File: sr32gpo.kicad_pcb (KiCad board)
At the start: 2 copper layers, 99.1 x 66 mm, 68 parts, among them J1 Power, J11 GPO, J12 GPO, J13 GND, J2 Power, J21 GPO, J22 GPO, J23 GND, J3 Power, J31 GPO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

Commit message: Redo with updated SOIC-16 footprint, better GND planes, and tentative fields for PCBWay assembly. Unverified.
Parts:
- U1, U2, U3, U4: footprint Package_SO:SO-16_3.9x9.9mm_P1.27mm -> Package_SO:SOIC-16_3.9x9.9mm_P1.27mm
- U11: value LD1117 -> LD1117V33
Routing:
- net /V+: track 47.1 -> 35.2 mm
- net VCC: track 155.3 -> 144.6 mm
- net /~{SRCLR}: track 81.4 -> 70.7 mm, vias 1 -> 0
- net GND: track 342.4 -> 352.2 mm, vias 1 -> 3
- net /RCLK: track 74.5 -> 67.8 mm, vias 1 -> 3
- net Net-(U1-Pad9): track 5.10 -> 10.9 mm
- net Net-(R22-Pad1): track 9.59 -> 4.58 mm
- net /~{OE}: track 62.5 -> 58.1 mm, vias 2 -> 1
- net Net-(U3-Pad9): track 12.8 -> 9.38 mm, vias 0 -> 2
- net Net-(R11-Pad1): track 14.0 -> 12.3 mm, vias 0 -> 2
- net /SRCLK: track 73.3 -> 72.2 mm, vias 3 -> 2
- net Net-(R41-Pad1): track 20.9 -> 20.2 mm
- net Net-(R21-Pad1): track 14.6 -> 15.3 mm, vias 0 -> 2

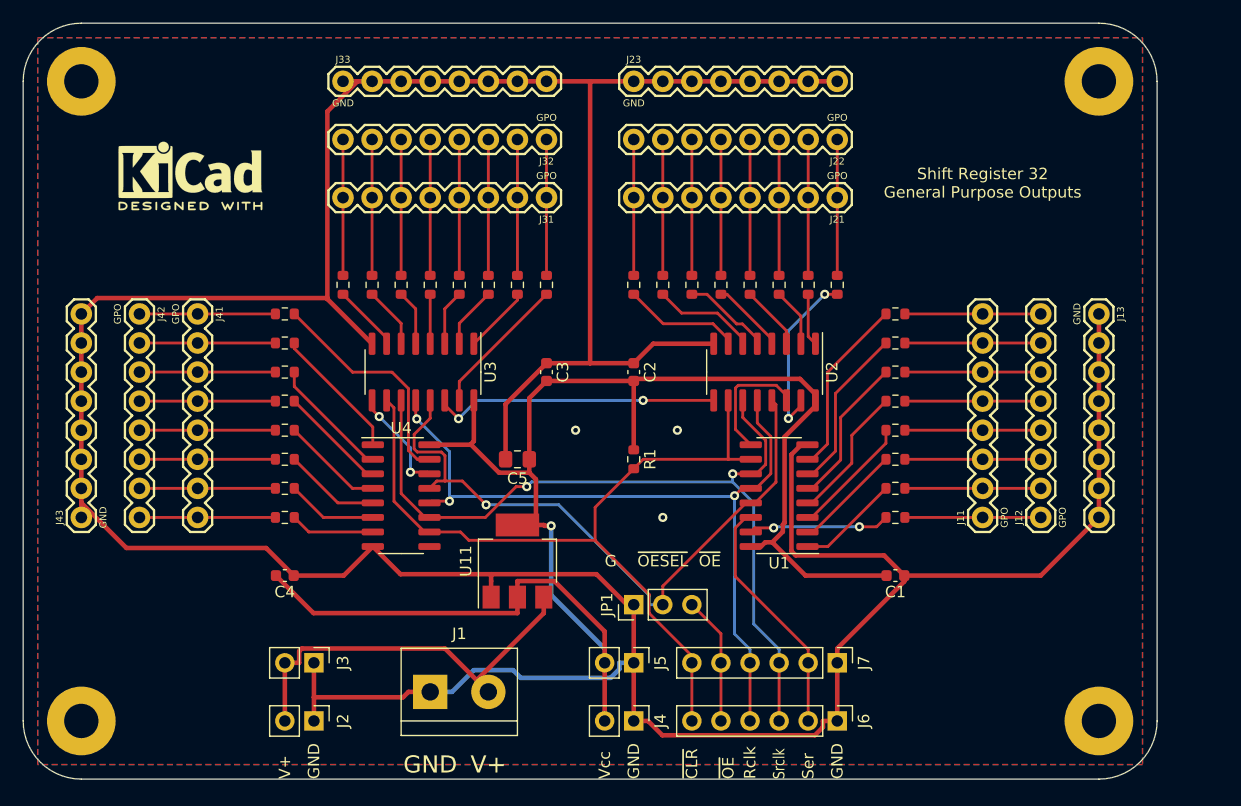
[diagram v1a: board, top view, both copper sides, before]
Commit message: Update to KiCad v8, improve silkscreen, generate BOM and POS files for PCBWay
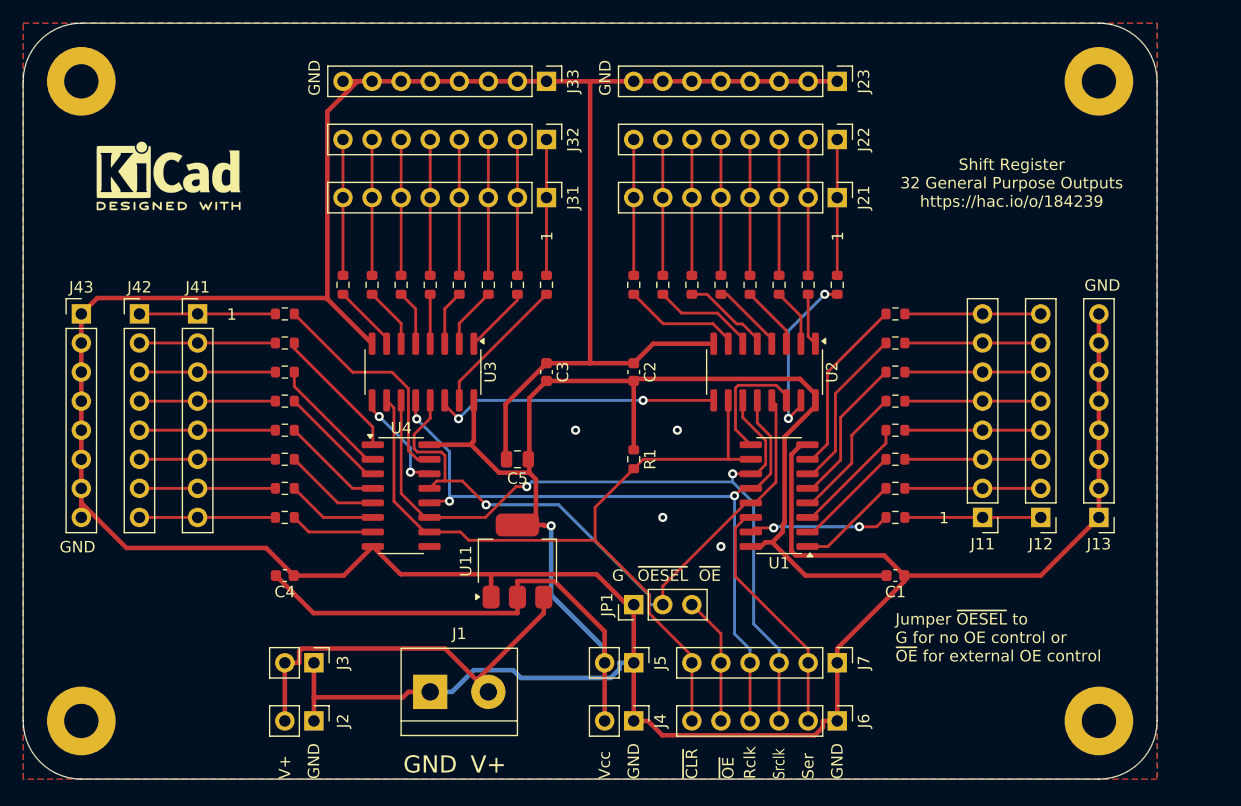
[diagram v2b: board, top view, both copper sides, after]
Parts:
- C5: footprint Capacitor_SMD:C_0805_2012Metric_Pad1.18x1.45mm_HandSolder -> Capacitor_SMD:C_0805_2012Metric
- J11, J12, J13, J21, J22, J23, J31, J32, J33, J41, J42, J43: footprint Connectors:1X08 -> Connector_PinHeader_2.54mm:PinHeader_1x08_P2.54mm_Vertical
- U11: value LD1117V33 -> LD1117V50
- moved J23 17.8 mm to (144.8, 45.7), turned to -90 degrees
- moved J33 17.8 mm to (119.4, 45.7), turned to -90 degrees
- moved J13 17.8 mm to (167.6, 83.8), turned to 180 degrees
- moved J43 17.8 mm to (78.7, 66.0), turned to 0 degrees
- moved REF** 1.91 mm to (86.4, 54.0)
- turned J11 to 180 degrees
- turned J12 to 180 degrees
- turned J21 to -90 degrees
- turned J22 to -90 degrees
- turned J31 to -90 degrees
- turned J32 to -90 degrees
- turned J41 to 0 degrees
- turned J42 to 0 degrees
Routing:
- net GND: vias 3 -> 4
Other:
- board text added: "1"
- board text added: "Jumper ~{OESEL} to G for no OE control or ~{OE} for external OE control"
- board text added: "Shift Register 32 General Purpose Outputs https://hac.io/o/184239"
- board text removed: "Shift Register 32 General Purpose Outputs"
